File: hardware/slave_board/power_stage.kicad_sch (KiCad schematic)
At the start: 27 parts, among them Q1 IRFP250N, Q2 IRFP250N, U1 LM358

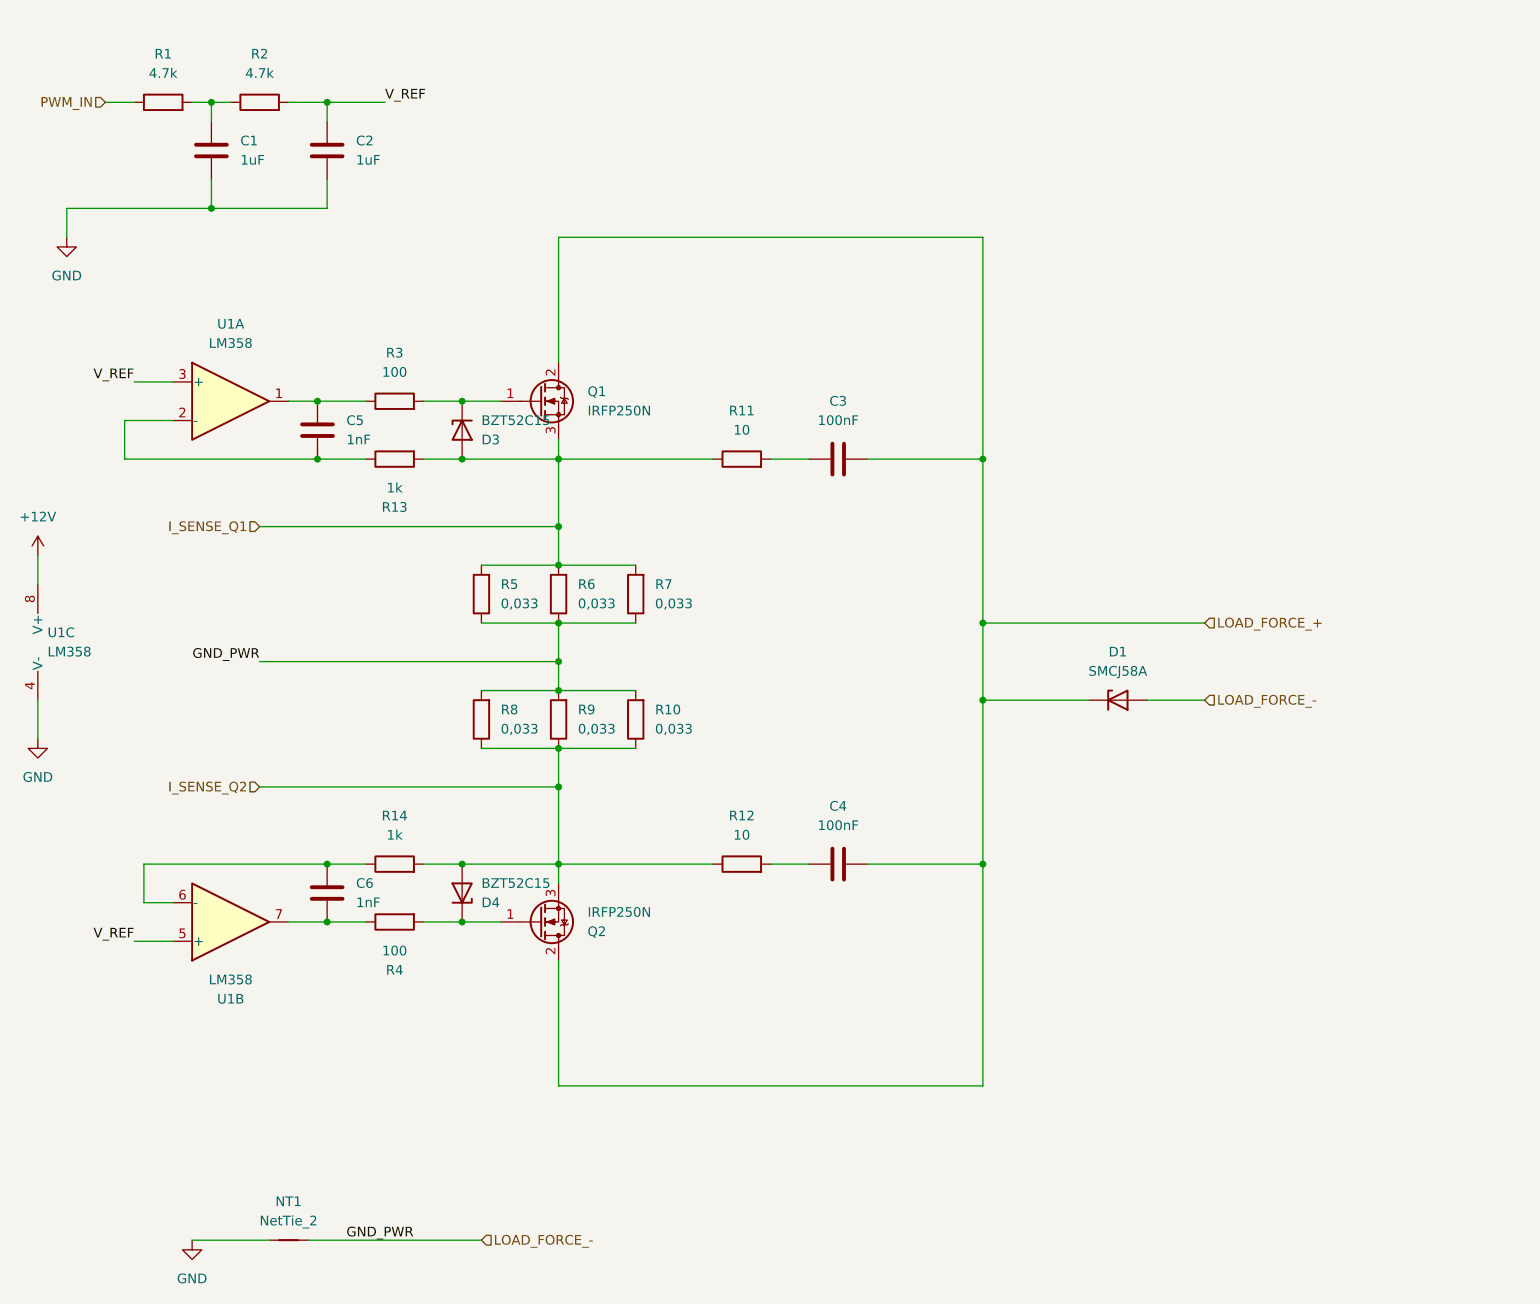
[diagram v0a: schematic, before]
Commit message: feat(hw): add Master-board RJ45 protection circuit with PTC and BAT54S clamps
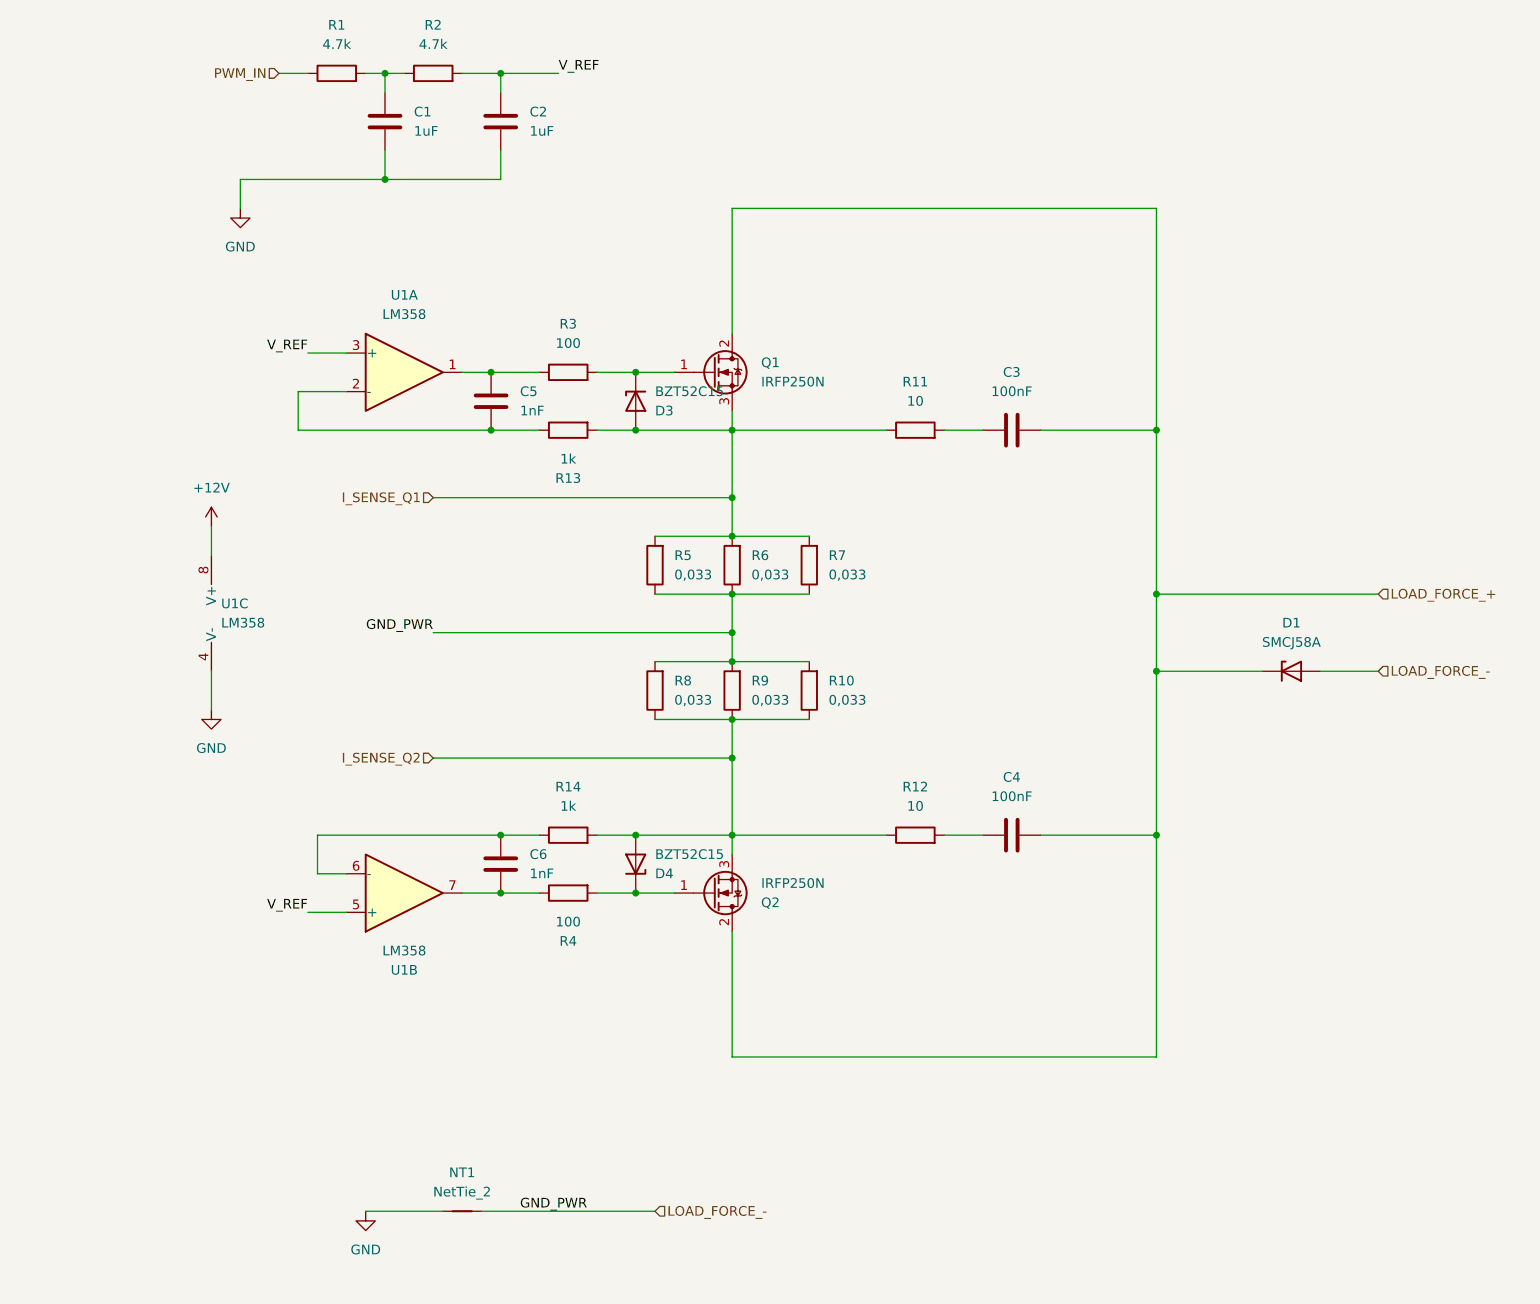
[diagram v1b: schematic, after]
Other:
- moved on the sheet: C1, C2, C3, C4, C5, C6, D1, D3, D4, NT1, Q1, Q2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

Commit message: hw(slave): fix footprints, enforce HandSolder, defer connector selection
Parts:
- C1, C2: footprint (none) -> Capacitor_SMD:C_0805_2012Metric_Pad1.18x1.45mm_HandSolder
- C3, C4: footprint Diode_SMD:Nexperia_DSN1608-2_1.6x0.8mm -> Capacitor_SMD:C_1206_3216Metric_Pad1.33x1.80mm_HandSolder
- C5, C6: footprint Capacitor_SMD:C_0805_2012Metric -> Capacitor_SMD:C_0805_2012Metric_Pad1.18x1.45mm_HandSolder
- D1: footprint Diode_SMD:D_SMC -> Diode_SMD:D_SMC-RM10_Universal_Handsoldering
- R1, R2, R4: footprint (none) -> Resistor_SMD:R_0805_2012Metric_Pad1.20x1.40mm_HandSolder
- R11, R12: footprint Package_TO_SOT_THT:TO-247-3_Vertical -> Resistor_SMD:R_1206_3216Metric_Pad1.30x1.75mm_HandSolder
- R13, R14: footprint Resistor_SMD:R_0805_2012Metric -> Resistor_SMD:R_0805_2012Metric_Pad1.20x1.40mm_HandSolder
- R3: footprint Package_TO_SOT_THT:TO-247-3_Vertical -> Resistor_SMD:R_0805_2012Metric_Pad1.20x1.40mm_HandSolder
- U1: footprint (none) -> Package_SO:SOIC-8_3.9x4.9mm_P1.27mm
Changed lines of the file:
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@@
 	)
 	(junction
+		(at 102.87 179.07)
+		(diameter 0)
+		(color 0 0 0 0)
+	)
+	(junction
 		(at 82.55 29.21)
 		(diameter 0)
@@
 	(wire
 		(pts
+			(xy 102.87 179.07) (xy 102.87 184.15)
+		)
+		(stroke
+			(width 0)
+			(type default)
+		)
+	)
+	(wire
+		(pts
 			(xy 67.31 29.21) (xy 67.31 31.75)
 		)
@@
 	(wire
 		(pts
+			(xy 102.87 173.99) (xy 102.87 179.07)
+		)
+		(stroke
+			(width 0)
+			(type default)
+		)
+	)
+	(wire
+		(pts
 			(xy 87.63 76.2) (xy 81.28 76.2)
 		)
@@
 	(wire
 		(pts
+			(xy 104.14 173.99) (xy 102.87 173.99)
+		)
+		(stroke
+			(width 0)
+			(type default)
+		)
+	)
+	(wire
+		(pts
 			(xy 140.97 129.54) (xy 146.05 129.54)
 		)
@@
 		)
 	)
-	(label "GND_PWR"
-		(at 85.09 179.07 0)
+	(label "V_REF"
+		(at 57.15 139.7 180)
 		(effects
 			(font
 				(size 1.27 1.27)
 			)
-			(justify left bottom)
+			(justify right bottom)
 		)
 	)
 	(label "V_REF"
-		(at 57.15 139.7 180)
+		(at 90.17 29.21 0)
 		(effects
 			(font
 				(size 1.27 1.27)
 			)
-			(justify right bottom)
+			(justify left bottom)
 		)
 	)
-	(label "V_REF"
-		(at 90.17 29.21 0)
+	(label "GND_PWR"
+		(at 102.87 184.15 0)
 		(effects
 			(font
@@
 	(hierarchical_label "LOAD_FORCE_-"
 		(shape input)
-		(at 102.87 179.07 0)
+		(at 104.14 173.99 0)
 		(effects
 			(font
@@
 			)
 		)
-		(property "Footprint" "Diode_SMD:Nexperia_DSN1608-2_1.6x0.8mm"
+		(property "Footprint" "Capacitor_SMD:C_1206_3216Metric_Pad1.33x1.80mm_HandSolder"
 			(at 153.67 128.5748 0)
 			(hide yes)
@@
 			)
 		)
-		(property "Description" "Плівковий, на 100V+"
+		(property "Description" "Ceramic Capacitor SMD 100nF, 100V, X7R, 1206"
 			(at 149.86 129.54 0)
 			(hide yes)
@@
 			)
 		)
-		(property "Footprint" "Diode_SMD:D_SMC"
+		(property "Footprint" "Diode_SMD:D_SMC-RM10_Universal_Handsoldering"
 			(at 186.69 112.395 0)
 			(hide yes)
@@
 			)
 		)
-		(property "Footprint" ""
+		(property "Footprint" "Capacitor_SMD:C_0805_2012Metric_Pad1.18x1.45mm_HandSolder"
 			(at 83.5152 39.37 0)
 			(hide yes)
@@
 			)
 		)
-		(property "Description" "C_PWM2"
+		(property "Description" "Ceramic Capacitor SMD 1uF, 50V, X7R, 0805"
 			(at 82.55 35.56 0)
 			(hide yes)
@@
 			)
 		)
-		(property "Footprint" "Resistor_SMD:R_0805_2012Metric"
+		(property "Footprint" "Resistor_SMD:R_0805_2012Metric_Pad1.20x1.40mm_HandSolder"
 			(at 91.44 131.318 90)
 			(hide yes)
@@
 			)
 		)
-		(property "Description" "Resistor SMD 0805"
+		(property "Description" "SMD Resistor 1kOhm, 1%, 0805"
 			(at 91.44 129.54 0)
 			(hide yes)
@@
 			)
 		)
-		(property "Description" "Resistor"
+		(property "Description" "Precision Current Sense Resistor SMD 33mOhm (0.033 Ohm), 1%, 2W, 2512"
 			(at 113.03 110.49 0)
 			(hide yes)
@@
 			)
 		)
-		(property "Footprint" ""
+		(property "Footprint" "Capacitor_SMD:C_0805_2012Metric_Pad1.18x1.45mm_HandSolder"
 			(at 68.2752 39.37 0)
 			(hide yes)
@@
 			)
 		)
-		(property "Description" "C_PWM1"
+		(property "Description" "Ceramic Capacitor SMD 1uF, 50V, X7R, 0805"
 			(at 67.31 35.56 0)
 			(hide yes)
@@
 			)
 		)
-		(property "Footprint" ""
+		(property "Footprint" "Resistor_SMD:R_0805_2012Metric_Pad1.20x1.40mm_HandSolder"
 			(at 73.66 30.988 90)
 			(hide yes)
@@
 			)
 		)
-		(property "Description" "R_PWM2"
+		(property "Description" "SMD Resistor 4.7kOhm, 1%, 0805"
 			(at 73.66 29.21 0)
 			(hide yes)
@@
 			)
 		)
-		(property "Description" "Resistor"
+		(property "Description" "Precision Current Sense Resistor SMD 33mOhm (0.033 Ohm), 1%, 2W, 2512"
 			(at 102.87 110.49 0)
 			(hide yes)
@@
 			)
 		)
-		(property "Description" "Resistor"
+		(property "Description" "Precision Current Sense Resistor SMD 33mOhm (0.033 Ohm), 1%, 2W, 2512"
 			(at 123.19 110.49 0)
 			(hide yes)
@@
 			)
 		)
-		(property "Footprint" "Package_TO_SOT_THT:TO-247-3_Vertical"
+		(property "Footprint" "Resistor_SMD:R_0805_2012Metric_Pad1.20x1.40mm_HandSolder"
 			(at 91.44 70.358 90)
 			(hide yes)
@@
 			)
 		)
-		(property "Description" "Resistor"
+		(property "Description" "SMD Resistor 100 Ohm, 1%, 0805"
 			(at 91.44 68.58 0)
 			(hide yes)
@@
 			)
 		)
-		(property "Footprint" ""
+		(property "Footprint" "Package_SO:SOIC-8_3.9x4.9mm_P1.27mm"
 			(at 46.99 100.33 0)
 			(hide yes)
@@
 			)
 		)
-		(property "Footprint" ""
+		(property "Footprint" "Resistor_SMD:R_0805_2012Metric_Pad1.20x1.40mm_HandSolder"
 			(at 91.44 135.382 90)
 			(hide yes)
@@
 			)
 		)
-		(property "Description" "Resistor"
+		(property "Description" "SMD Resistor 100 Ohm, 1%, 0805"
 			(at 91.44 137.16 0)
 			(hide yes)
@@
 			)
 		)
-		(property "Footprint" "Capacitor_SMD:C_0805_2012Metric"
+		(property "Footprint" "Capacitor_SMD:C_0805_2012Metric_Pad1.18x1.45mm_HandSolder"
 			(at 83.5152 137.16 0)
 			(hide yes)
@@
 			)
 		)
-		(property "Description" "Capacitor_SMD:C_0805"
+		(property "Description" "Ceramic Capacitor SMD 1nF, 50V, C0G/NP0, 0805"
 			(at 82.55 133.35 0)
 			(hide yes)
@@
 			)
 		)
-		(property "Description" "Resistor"
+		(property "Description" "Precision Current Sense Resistor SMD 33mOhm (0.033 Ohm), 1%, 2W, 2512"
 			(at 123.19 93.98 0)
 			(hide yes)
@@
 			)
 		)
-		(property "Footprint" "Package_TO_SOT_THT:TO-247-3_Vertical"
+		(property "Footprint" "Resistor_SMD:R_1206_3216Metric_Pad1.30x1.75mm_HandSolder"
 			(at 137.16 131.318 90)
 			(hide yes)
@@
 			)
 		)
-		(property "Description" "Resistor"
+		(property "Description" "SMD Resistor 10 Ohm, 0.25W, 1%, 1206"
 			(at 137.16 129.54 0)
 			(hide yes)
@@
 			)
 		)
-		(property "Footprint" "Resistor_SMD:R_0805_2012Metric"
+		(property "Footprint" "Resistor_SMD:R_0805_2012Metric_Pad1.20x1.40mm_HandSolder"
 			(at 91.44 74.422 90)
 			(hide yes)
@@
 			)
 		)
-		(property "Description" "Resistor SMD 0805"
+		(property "Description" "SMD Resistor 1kOhm, 1%, 0805"
 			(at 91.44 76.2 0)
 			(hide yes)
@@
 			)
 		)
-		(property "Footprint" ""
+		(property "Footprint" "Resistor_SMD:R_0805_2012Metric_Pad1.20x1.40mm_HandSolder"
 			(at 60.96 30.988 90)
 			(hide yes)
@@
 			)
 		)
-		(property "Description" "R_PWM1"
+		(property "Description" "SMD Resistor 4.7kOhm, 1%, 0805"
 			(at 60.96 29.21 0)
 			(hide yes)
@@
 			)
 		)
-		(property "Footprint" "Package_TO_SOT_THT:TO-247-3_Vertical"
+		(property "Footprint" "Resistor_SMD:R_1206_3216Metric_Pad1.30x1.75mm_HandSolder"
 			(at 137.16 77.978 90)
 			(hide yes)
@@
 			)
 		)
-		(property "Description" "Resistor"
+		(property "Description" "SMD Resistor 10 Ohm, 0.25W, 1%, 1206"
 			(at 137.16 76.2 0)
 			(hide yes)
@@
 			)
 		)
-		(property "Footprint" ""
+		(property "Footprint" "Package_SO:SOIC-8_3.9x4.9mm_P1.27mm"
 			(at 69.85 68.58 0)
 			(hide yes)
@@
 			)
 		)
-		(property "Footprint" "Diode_SMD:Nexperia_DSN1608-2_1.6x0.8mm"
+		(property "Footprint" "Capacitor_SMD:C_1206_3216Metric_Pad1.33x1.80mm_HandSolder"
 			(at 153.67 75.2348 0)
 			(hide yes)
@@
 			)
 		)
-		(property "Description" "Плівковий, на 100V+"
+		(property "Description" "Ceramic Capacitor SMD 100nF, 100V, X7R, 1206"
 			(at 149.86 76.2 0)
 			(hide yes)
@@
 			)
 		)
-		(property "Description" "Resistor"
+		(property "Description" "Precision Current Sense Resistor SMD 33mOhm (0.033 Ohm), 1%, 2W, 2512"
 			(at 102.87 93.98 0)
 			(hide yes)
@@
 			)
 		)
-		(property "Footprint" ""
+		(property "Footprint" "Package_SO:SOIC-8_3.9x4.9mm_P1.27mm"
 			(at 69.85 137.16 0)
 			(hide yes)
@@
 			)
 		)
-		(property "Footprint" "Capacitor_SMD:C_0805_2012Metric"
+		(property "Footprint" "Capacitor_SMD:C_0805_2012Metric_Pad1.18x1.45mm_HandSolder"
 			(at 82.2452 76.2 0)
 			(hide yes)
@@
 			)
 		)
-		(property "Description" "Capacitor_SMD:C_0805"
+		(property "Description" "Ceramic Capacitor SMD 1nF, 50V, C0G/NP0, 0805"
 			(at 81.28 72.39 0)
 			(hide yes)
@@
 			)
 		)
-		(property "Description" "Resistor"
+		(property "Description" "Precision Current Sense Resistor SMD 33mOhm (0.033 Ohm), 1%, 2W, 2512"
 			(at 113.03 93.98 0)
 			(hide yes)

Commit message: Implement cooling sheet, fan control, and update power connectors
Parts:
- R10, R5, R6, R7, R8, R9: value 0,033 -> 0.033
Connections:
- net LOAD_FORCE_- renamed GND_PWR
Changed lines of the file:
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@@
+	(wire
+		(pts
+			(xy 102.87 184.15) (xy 104.14 184.15)
+		)
+		(stroke
+			(width 0)
+			(type default)
+		)
+	)
 	(wire
 		(pts
@@
 		)
 	)
-	(label "GND_PWR"
-		(at 73.66 102.87 180)
-		(effects
-			(font
-				(size 1.27 1.27)
-			)
-			(justify right bottom)
-		)
-	)
 	(label "V_REF"
 		(at 57.15 139.7 180)
@@
 		)
 	)
-	(label "GND_PWR"
-		(at 102.87 184.15 0)
+	(global_label "I_SENSE_Q2"
+		(shape input)
+		(at 73.66 119.38 180)
+		(fields_autoplaced yes)
 		(effects
 			(font
 				(size 1.27 1.27)
 			)
-			(justify left bottom)
-		)
-	)
-	(hierarchical_label "LOAD_FORCE_-"
+			(justify right)
+		)
+		(property "Intersheetrefs" "${INTERSHEET_REFS}"
+			(at 59.5473 119.38 0)
+			(hide yes)
+			(show_name no)
+			(do_not_autoplace no)
+			(effects
+				(font
+					(size 1.27 1.27)
+				)
+				(justify right)
+			)
+		)
+	)
+	(global_label "LOAD_FORCE_-"
 		(shape input)
-		(at 198.12 107.95 0)
+		(at 104.14 173.99 0)
+		(fields_autoplaced yes)
 		(effects
 			(font
@@
 			(justify left)
 		)
-	)
-	(hierarchical_label "LOAD_FORCE_-"
+		(property "Intersheetrefs" "${INTERSHEET_REFS}"
+			(at 121.4581 173.99 0)
+			(hide yes)
+			(show_name no)
+			(do_not_autoplace no)
+			(effects
+				(font
+					(size 1.27 1.27)
+				)
+				(justify left)
+			)
+		)
+	)
+	(global_label "I_SENSE_Q1"
 		(shape input)
-		(at 104.14 173.99 0)
+		(at 73.66 85.09 180)
+		(fields_autoplaced yes)
 		(effects
 			(font
 				(size 1.27 1.27)
 			)
-			(justify left)
-		)
-	)
-	(hierarchical_label "LOAD_FORCE_+"
+			(justify right)
+		)
+		(property "Intersheetrefs" "${INTERSHEET_REFS}"
+			(at 59.5473 85.09 0)
+			(hide yes)
+			(show_name no)
+			(do_not_autoplace no)
+			(effects
+				(font
+					(size 1.27 1.27)
+				)
+				(justify right)
+			)
+		)
+	)
+	(global_label "LOAD_FORCE_-"
 		(shape input)
-		(at 198.12 97.79 0)
+		(at 198.12 107.95 0)
+		(fields_autoplaced yes)
 		(effects
 			(font
@@
 			)
 			(justify left)
+		)
+		(property "Intersheetrefs" "${INTERSHEET_REFS}"
+			(at 215.4381 107.95 0)
+			(hide yes)
+			(show_name no)
+			(do_not_autoplace no)
+			(effects
+				(font
+					(size 1.27 1.27)
+				)
+				(justify left)
+			)
+		)
+	)
+	(global_label "GND_PWR"
+		(shape input)
+		(at 104.14 184.15 0)
+		(fields_autoplaced yes)
+		(effects
+			(font
+				(size 1.27 1.27)
+			)
+			(justify left)
+		)
+		(property "Intersheetrefs" "${INTERSHEET_REFS}"
+			(at 115.9547 184.15 0)
+			(hide yes)
+			(show_name no)
+			(do_not_autoplace no)
+			(effects
+				(font
+					(size 1.27 1.27)
+				)
+				(justify left)
+			)
+		)
+	)
+	(global_label "LOAD_FORCE_+"
+		(shape input)
+		(at 198.12 97.79 0)
+		(fields_autoplaced yes)
+		(effects
+			(font
+				(size 1.27 1.27)
+			)
+			(justify left)
+		)
+		(property "Intersheetrefs" "${INTERSHEET_REFS}"
+			(at 215.4381 97.79 0)
+			(hide yes)
+			(show_name no)
+			(do_not_autoplace no)
+			(effects
+				(font
+					(size 1.27 1.27)
+				)
+				(justify left)
+			)
+		)
+	)
+	(global_label "GND_PWR"
+		(shape input)
+		(at 73.66 102.87 180)
+		(fields_autoplaced yes)
+		(effects
+			(font
+				(size 1.27 1.27)
+			)
+			(justify right)
+		)
+		(property "Intersheetrefs" "${INTERSHEET_REFS}"
+			(at 61.8453 102.87 0)
+			(hide yes)
+			(show_name no)
+			(do_not_autoplace no)
+			(effects
+				(font
+					(size 1.27 1.27)
+				)
+				(justify right)
+			)
 		)
 	)
@@
 		)
 	)
-	(hierarchical_label "I_SENSE_Q2"
-		(shape input)
-		(at 73.66 119.38 180)
-		(effects
-			(font
-				(size 1.27 1.27)
-			)
-			(justify right)
-		)
-	)
-	(hierarchical_label "I_SENSE_Q1"
-		(shape input)
-		(at 73.66 85.09 180)
-		(effects
-			(font
-				(size 1.27 1.27)
-			)
-			(justify right)
-		)
-	)
 	(symbol
 		(lib_id "Device:D_Zener")
@@
 			)
 		)
-		(property "Value" "0,033"
+		(property "Value" "0.033"
 			(at 115.57 111.7599 0)
 			(show_name no)
@@
 			)
 		)
-		(property "Value" "0,033"
+		(property "Value" "0.033"
 			(at 105.41 111.7599 0)
 			(show_name no)
@@
 			)
 		)
-		(property "Value" "0,033"
+		(property "Value" "0.033"
 			(at 125.73 111.7599 0)
 			(show_name no)
@@
 			)
 		)
-		(property "Value" "0,033"
+		(property "Value" "0.033"
 			(at 125.73 95.2499 0)
 			(show_name no)
@@
 			)
 		)
-		(property "Value" "0,033"
+		(property "Value" "0.033"
 			(at 105.41 95.2499 0)
 			(show_name no)
@@
 			)
 		)
-		(property "Value" "0,033"
+		(property "Value" "0.033"
 			(at 115.57 95.2499 0)
 			(show_name no)
